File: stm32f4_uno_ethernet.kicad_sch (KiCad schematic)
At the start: 11 parts, among them J101 STM32 GPIO, J102 Digital/PWM, J103 STM32 GPIO, J104 STM32 GPIO, J105 STM32 GPIO, J106 Power, J107 Ethernet, J108 STM32 GPIO, J109 Digital/PWM, J110 Analog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

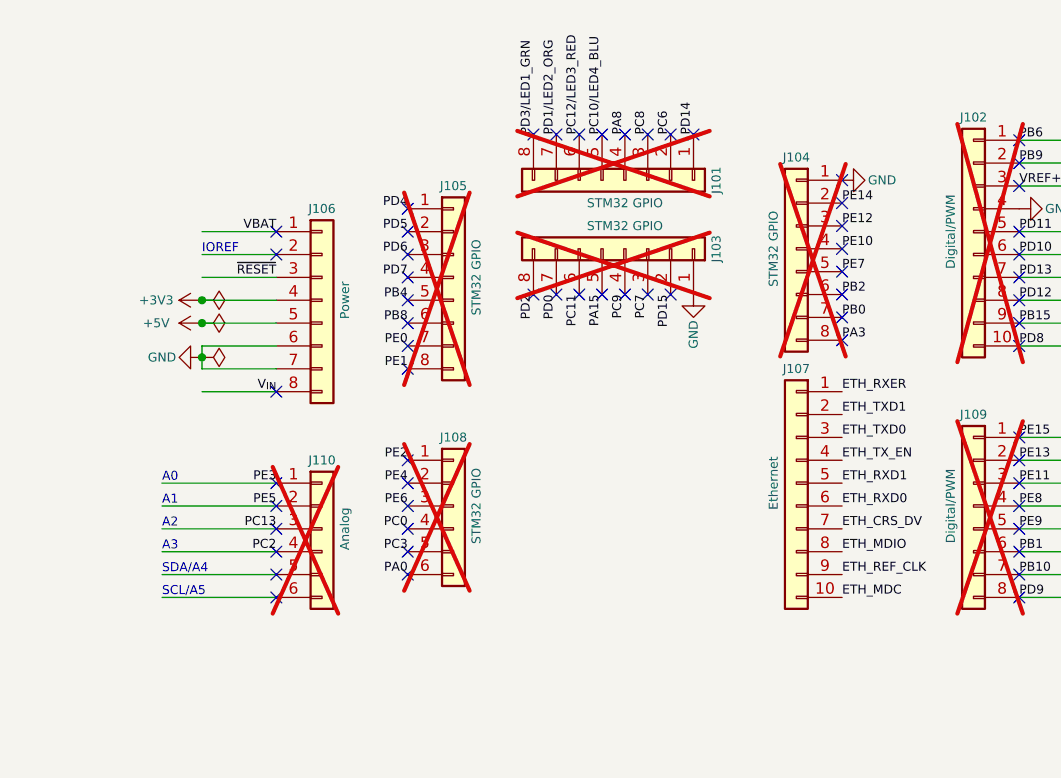
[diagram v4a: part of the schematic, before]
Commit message: Release 1.0.0 sent to JLCPCB
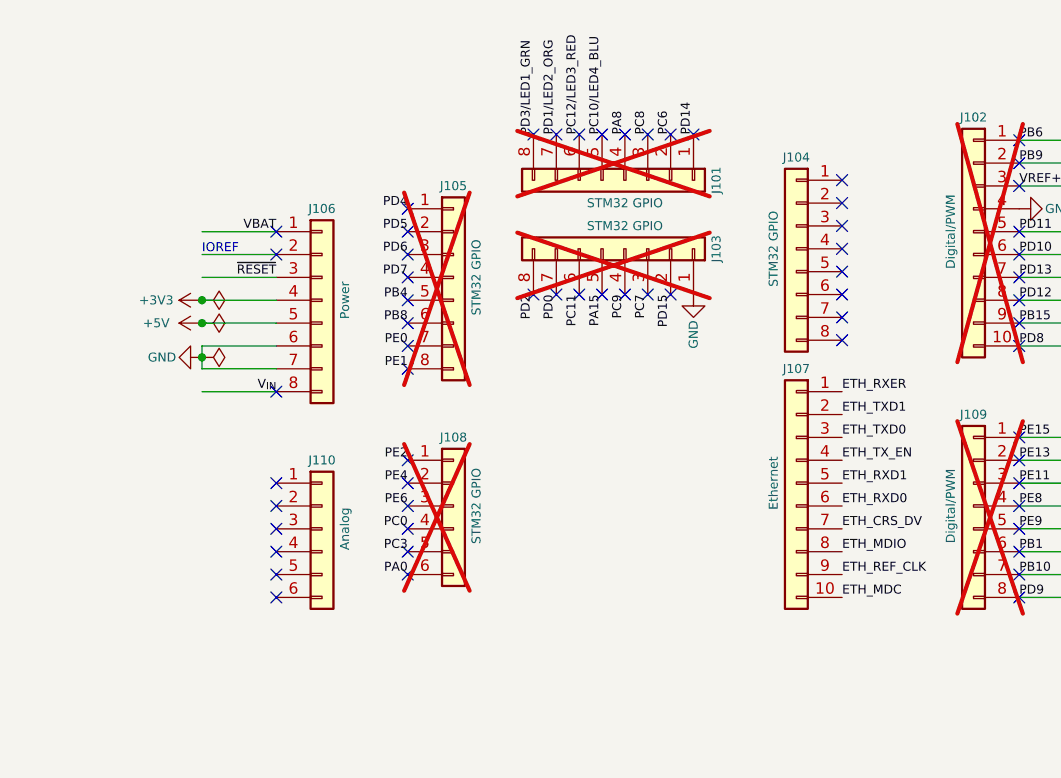
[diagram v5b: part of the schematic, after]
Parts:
- J104, J110: now fitted
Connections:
- net GND: no longer J104.1 (Pin_1)
- net PA3: no longer names the net of J104.8 (Pin_8)
- net PB0: no longer names the net of J104.7 (Pin_7)
- net PB2: no longer names the net of J104.6 (Pin_6)
- net PC13: no longer names the net of J110.3 (Pin_3)
- net PC2: no longer names the net of J110.4 (Pin_4)
- net PE10: no longer names the net of J104.4 (Pin_4)
- net PE12: no longer names the net of J104.3 (Pin_3)
- net PE14: no longer names the net of J104.2 (Pin_2)
- net PE3: no longer names the net of J110.1 (Pin_1)
- net PE5: no longer names the net of J110.2 (Pin_2)
- net PE7: no longer names the net of J104.5 (Pin_5)
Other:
- note removed: "A0"
- note removed: "A1"
- note removed: "A2"
- note removed: "A3"
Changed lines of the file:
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@@
     (title "STM32F4 Uno Ethernet")
     (date "2023-10-02")
-    (rev "1.0.x-dev")
+    (rev "1.0.0")
     (company "easy-smart solution GmbH")
   )
@@
     (stroke (width 0) (type default))
   )
-  (wire (pts (xy 172.085 78.105) (xy 184.785 78.105))
-    (stroke (width 0) (type solid))
-  )
   (wire (pts (xy 176.53 50.165) (xy 176.53 51.435))
     (stroke (width 0) (type default))
@@
     (stroke (width 0) (type solid))
   )
-  (wire (pts (xy 184.785 65.405) (xy 172.085 65.405))
-    (stroke (width 0) (type solid))
-  )
   (wire (pts (xy 267.335 40.005) (xy 280.035 40.005))
     (stroke (width 0) (type solid))
@@
     (stroke (width 0) (type solid))
   )
-  (wire (pts (xy 184.785 70.485) (xy 172.085 70.485))
-    (stroke (width 0) (type solid))
-  )
   (wire (pts (xy 59.69 64.77) (xy 63.5 64.77))
     (stroke (width 0) (type default))
   )
-  (wire (pts (xy 172.085 67.945) (xy 184.785 67.945))
-    (stroke (width 0) (type solid))
-  )
   (wire (pts (xy 59.69 62.23) (xy 63.5 62.23))
     (stroke (width 0) (type default))
@@
     (stroke (width 0) (type solid))
   )
-  (wire (pts (xy 172.085 73.025) (xy 184.785 73.025))
-    (stroke (width 0) (type solid))
-  )
   (wire (pts (xy 127 63.5) (xy 131.445 63.5))
     (stroke (width 0) (type default))
@@
     (stroke (width 0) (type solid))
   )
-  (wire (pts (xy 184.785 75.565) (xy 172.085 75.565))
-    (stroke (width 0) (type solid))
-  )
   (wire (pts (xy 176.53 51.435) (xy 176.53 52.705))
     (stroke (width 0) (type default))
@@
     (stroke (width 0) (type solid))
   )
-  (text "A1" (at 172.085 67.945 0)
-    (effects (font (size 1 1)) (justify left bottom))
-  )
-  (text "SDA/A4" (at 172.085 75.565 0)
-    (effects (font (size 1 1)) (justify left bottom))
-  )
   (text "AREF" (at 280.035 32.385 0)
     (effects (font (size 1 1)) (justify right bottom))
@@
     (effects (font (size 1 1)) (justify right bottom))
   )
-  (text "A3" (at 172.085 73.025 0)
-    (effects (font (size 1 1)) (justify left bottom))
-  )
   (text "D4" (at 280.035 67.945 0)
     (effects (font (size 1 1)) (justify right bottom))
@@
   (text "SCL/A5" (at 280.035 27.305 0)
     (effects (font (size 1 1)) (justify right bottom))
-  )
-  (text "SCL/A5" (at 172.085 78.105 0)
-    (effects (font (size 1 1)) (justify left bottom))
-  )
-  (text "A0" (at 172.085 65.405 0)
-    (effects (font (size 1 1)) (justify left bottom))
   )
   (text "SDA/A4" (at 280.035 29.845 0)
@@
     (effects (font (size 1 1)) (justify right bottom))
   )
-  (text "A2" (at 172.085 70.485 0)
-    (effects (font (size 1 1)) (justify left bottom))
-  )
   (text "RX/D0" (at 280.035 78.105 0)
     (effects (font (size 1 1)) (justify right bottom))
@@
     (effects (font (size 1 1)) (justify right bottom))
   )
-  (label "PB2" (at 247.65 44.45 0) (fields_autoplaced)
-    (effects (font (size 1 1)) (justify left bottom))
-  )
   (label "PB15" (at 267.335 47.625 0) (fields_autoplaced)
     (effects (font (size 1 1)) (justify left bottom))
@@
     (effects (font (size 1 1)) (justify left bottom))
   )
-  (label "PE5" (at 184.785 67.945 180) (fields_autoplaced)
-    (effects (font (size 1 1)) (justify right bottom))
-  )
   (label "PE4" (at 199.39 65.405 180) (fields_autoplaced)
     (effects (font (size 1 1)) (justify right bottom))
   )
-  (label "PC13" (at 184.785 70.485 180) (fields_autoplaced)
-    (effects (font (size 1 1)) (justify right bottom))
-  )
   (label "ETH_RXD0" (at 131.445 63.5 0) (fields_autoplaced)
     (effects (font (size 1 1)) (justify left bottom))
@@
     (effects (font (size 1 1)) (justify left bottom))
   )
-  (label "PA3" (at 247.65 49.53 0) (fields_autoplaced)
-    (effects (font (size 1 1)) (justify left bottom))
-  )
   (label "PD7" (at 199.39 42.545 180) (fields_autoplaced)
     (effects (font (size 1 1)) (justify right bottom))
@@
     (effects (font (size 1 1)) (justify left bottom))
   )
-  (label "PE12" (at 247.65 36.83 0) (fields_autoplaced)
-    (effects (font (size 1 1)) (justify left bottom))
-  )
   (label "PD14" (at 231.14 26.67 90) (fields_autoplaced)
     (effects (font (size 1 1)) (justify left bottom))
@@
     (effects (font (size 1 1)) (justify right bottom))
   )
-  (label "PE14" (at 247.65 34.29 0) (fields_autoplaced)
-    (effects (font (size 1 1)) (justify left bottom))
-  )
   (label "ETH_CRS_DV" (at 131.445 66.04 0) (fields_autoplaced)
     (effects (font (size 1 1)) (justify left bottom))
@@
     (effects (font (size 1 1)) (justify left bottom))
   )
-  (label "PE7" (at 247.65 41.91 0) (fields_autoplaced)
-    (effects (font (size 1 1)) (justify left bottom))
-  )
   (label "VREF+" (at 267.335 32.385 0) (fields_autoplaced)
     (effects (font (size 1 1)) (justify left bottom))
   )
-  (label "PE3" (at 184.785 65.405 180) (fields_autoplaced)
-    (effects (font (size 1 1)) (justify right bottom))
-  )
   (label "PB4" (at 199.39 45.085 180) (fields_autoplaced)
     (effects (font (size 1 1)) (justify right bottom))
@@
     (effects (font (size 1 1)) (justify left bottom))
   )
-  (label "PB0" (at 247.65 46.99 0) (fields_autoplaced)
-    (effects (font (size 1 1)) (justify left bottom))
-  )
   (label "PD10" (at 267.335 40.005 0) (fields_autoplaced)
     (effects (font (size 1 1)) (justify left bottom))
   )
-  (label "PE10" (at 247.65 39.37 0) (fields_autoplaced)
-    (effects (font (size 1 1)) (justify left bottom))
-  )
   (label "PD6" (at 199.39 40.005 180) (fields_autoplaced)
     (effects (font (size 1 1)) (justify right bottom))
@@
   )
   (label "PA15" (at 220.98 44.45 270) (fields_autoplaced)
-    (effects (font (size 1 1)) (justify right bottom))
-  )
-  (label "PC2" (at 184.785 73.025 180) (fields_autoplaced)
     (effects (font (size 1 1)) (justify right bottom))
   )
@@
   )
   (symbol (lib_id "Connector_Generic:Conn_01x06") (at 189.865 70.485 0) (unit 1)
-    (in_bom no) (on_board yes) (dnp yes)
+    (in_bom no) (on_board yes) (dnp no)
     (property "Reference" "J110" (at 189.865 62.865 0)
       (effects (font (size 1 1)))
@@
   )
   (symbol (lib_id "Connector_Generic:Conn_01x08") (at 242.57 39.37 0) (mirror y) (unit 1)
-    (in_bom no) (on_board yes) (dnp yes)
+    (in_bom no) (on_board yes) (dnp no)
     (property "Reference" "J104" (at 242.57 29.21 0)
       (effects (font (size 1 1)))
@@
         )
       )
-    )
-  )
-  (symbol (lib_id "power:GND") (at 247.65 31.75 90) (unit 1)
-    (in_bom yes) (on_board yes) (dnp no)
-    (property "Reference" "#PWR0107" (at 254 31.75 0)
-      (effects (font (size 1 1)) hide)
-    )
-    (property "Value" "GND" (at 252.095 31.75 90)
-      (effects (font (size 1 1)))
-    )
-    (property "Footprint" "" (at 247.65 31.75 0)
-      (effects (font (size 1 1)))
-    )
-    (property "Datasheet" "" (at 247.65 31.75 0)
-      (effects (font (size 1 1)))
-    )
-    (pin "1")
-    (instances
-      (project "stm32f4_uno_ethernet"
-        (path "/e63e39d7-6ac0-4ffd-8aa3-1841a4541b55"
-          (reference "#PWR0107") (unit 1)
-        )
-      )

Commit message: #4 Wrong polarity on C207
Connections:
- net +3V3: now also J106.2 (Pin_2)
- no-connect marks 63 -> 62
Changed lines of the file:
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@@
   (title_block
     (title "STM32F4 Uno Ethernet")
-    (date "2023-10-02")
-    (rev "1.0.0")
+    (date "2023-10-14")
+    (rev "1.0.x-dev")
     (company "easy-smart solution GmbH")
   )
@@
   (no_connect (at 184.785 70.485))
   (no_connect (at 184.785 78.105))
-  (no_connect (at 184.785 40.005))
   (no_connect (at 213.36 26.67))
   (no_connect (at 267.335 50.165))
@@
         )
       )
+    )
+  )
+  (symbol (lib_name "+3V3_1") (lib_id "power:+3V3") (at 176.53 40.005 90) (unit 1)
+    (in_bom yes) (on_board yes) (dnp no)
+    (property "Reference" "#PWR0107" (at 180.34 40.005 0)
+      (effects (font (size 1 1)) hide)
+    )
+    (property "Value" "+3V3" (at 171.45 40.005 90)
+      (effects (font (size 1 1)))
+    )
+    (property "Footprint" "" (at 176.53 40.005 0)
+      (effects (font (size 1 1)) hide)
+    )
+    (property "Datasheet" "" (at 176.53 40.005 0)
+      (effects (font (size 1 1)) hide)
+    )
+    (pin "1")
+    (instances
+      (project "stm32f4_uno_ethernet"
+        (path "/e63e39d7-6ac0-4ffd-8aa3-1841a4541b55"
+          (reference "#PWR0107") (unit 1)
+        )
+      )
